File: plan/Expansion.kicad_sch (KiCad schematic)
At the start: 0 parts

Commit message: Create Expansion schematic
Expansion for GPIOs on
- Castellated Pads
- Solder Pins
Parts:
- added J2: EFR32MG24_Core_Expansion_2x6, Smarthome:Module_EFR32MG24_Core_Castellated_2x6_PTH_P2.54mm, symbol Smarthome:EFR32MG24_Core_Expansion_2x6
- added TP1, TP10, TP11, TP12, TP13, TP14, TP15, TP16, TP17, TP18, TP19, TP2, TP20, TP21, TP22, TP3, TP4, TP5, TP6, TP7, TP8, TP9: GPIO_SolderPad, Smarthome:GPIO_SolderPad_D1.0mm_Bottom, symbol Smarthome:GPIO_SolderPad
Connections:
- new net GND: J2.1 (GND)
- new net PA00: TP1.1
- new net PA01: TP2.1
- new net PA02: TP3.1
- new net PA03: TP4.1
- new net PA04: TP5.1
- new net PA05: J2.10 (PA05)
- new net PA06: TP6.1
- new net PA07: TP7.1
- new net PA08: TP8.1
- new net PA09: TP9.1
- new net PB00: TP10.1
- new net PB01: J2.5 (PB01)
- new net PB02: TP11.1
- new net PB03: J2.11 (PB03)
- new net PB04: TP12.1
- new net PB05: TP13.1
- new net PC00: J2.2 (PC00)
- new net PC01: J2.6 (PC01)
- new net PC02: J2.12 (PC02)
- new net PC03: TP14.1
- new net PC04: TP15.1
- new net PC05: J2.8 (PC05)
- new net PC06: TP16.1
- new net PC07: J2.3 (PC07)
- new net PC08: TP17.1
- new net PC09: TP18.1
- new net PD00: TP19.1
- new net PD01: TP20.1
- new net PD02: J2.9 (PD02)
- new net PD03: TP21.1
- new net PD04: TP22.1
- new net PD05: J2.4 (PD05)
- new net VBAT: J2.7 (VBAT)
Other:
- note added: "Castellated Pads + PTH GND, VBATT, GPIOs (8x EM4-Wakeup, 2x normal)"
- note added: "PAIR BUTTON"
- note added: "PORT A"
- note added: "PORT B"
- note added: "PORT C"
- note added: "PORT D"
- note added: "STATUS LED"
- note added: "SWCLK"
- note added: "SWDIO"
- note added: "SWO"
- note added: "Solder Pads"

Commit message: Added information about shared GPIOs
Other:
- note added: "PA01 - SWCLK (shared) PA02 - SWDIO (shared) PA03 - SWO (shared) PC08 - Status LED (shared) PC09 - Pair Button (shared)"
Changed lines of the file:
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@@
 	(generator_version "10.0")
 	(paper "A4")
+	(text "PA01 - SWCLK (shared)\nPA02 - SWDIO (shared)\nPA03 - SWO (shared)\nPC08 - Status LED (shared)\nPC09 - Pair Button (shared)"
+		(exclude_from_sim no)
+		(at 72.39 134.62 0)
+		(effects
+			(font
+				(size 1.27 1.27)
+			)
+			(justify left)
+		)
+	)
 	(text "PORT C"
 		(exclude_from_sim no)

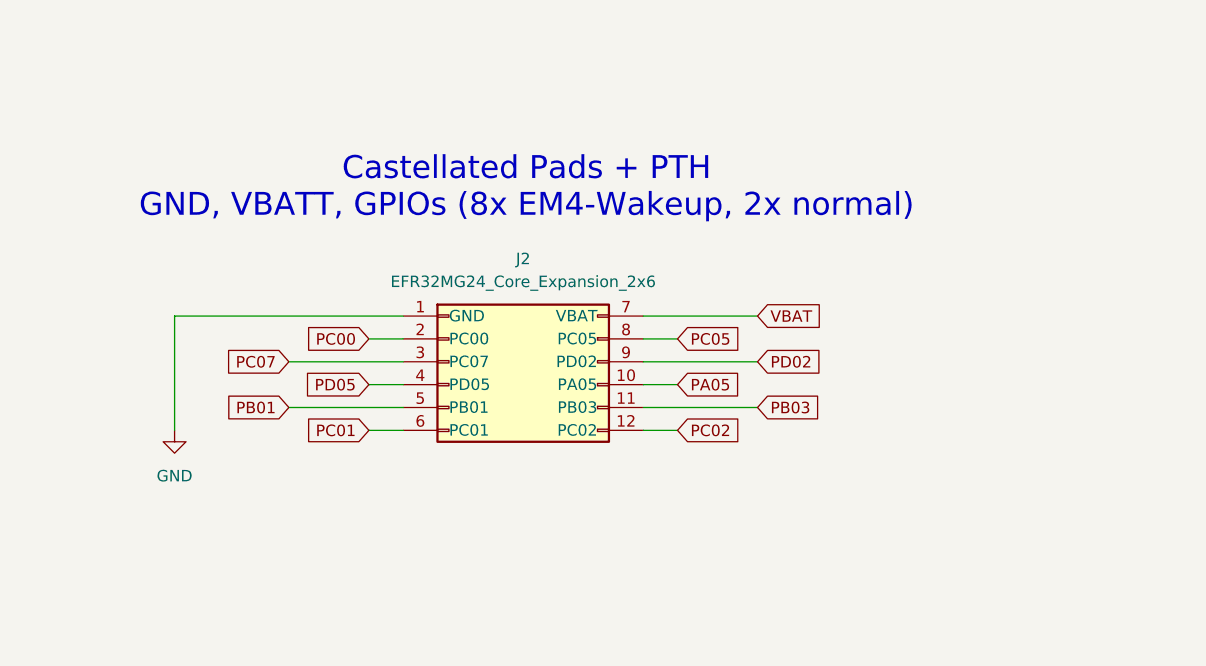
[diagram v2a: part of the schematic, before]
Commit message: Adjust and place Castellated Pads and THT connection
This implicitly defines the edge cuts of the board
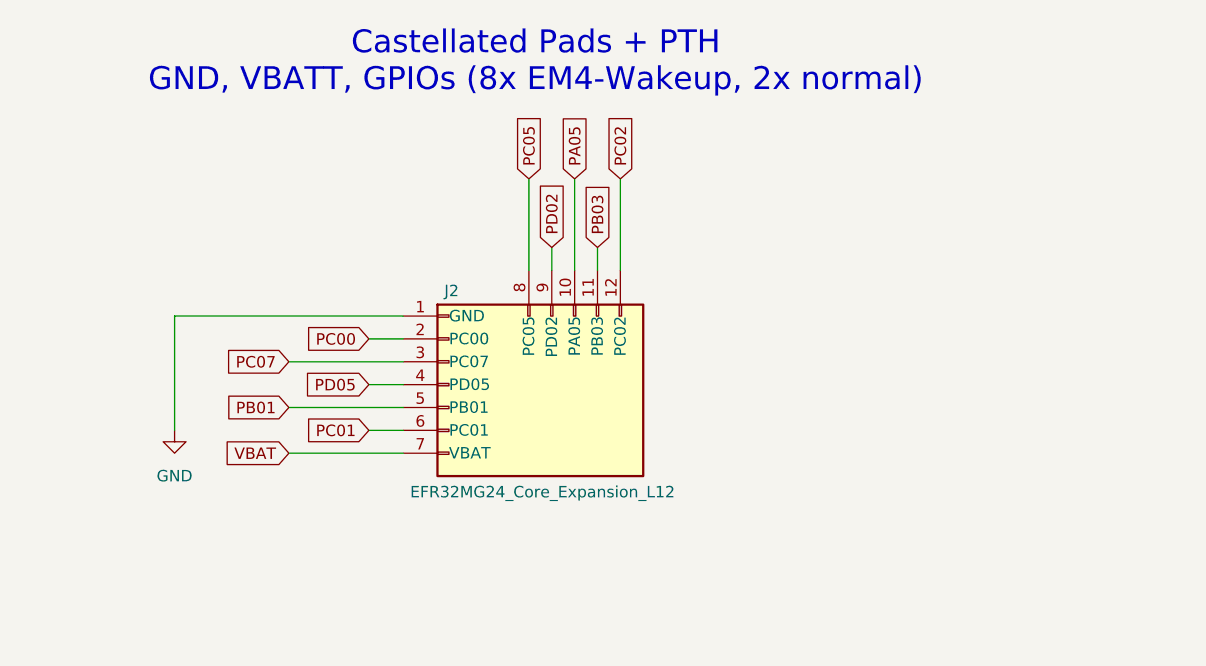
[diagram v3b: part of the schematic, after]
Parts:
- J2: value EFR32MG24_Core_Expansion_2x6 -> EFR32MG24_Core_Expansion_L12; footprint Smarthome:Module_EFR32MG24_Core_Castellated_2x6_PTH_P2.54mm -> Smarthome:Module_EFR32MG24_Core_Castellated_L_12Pin_P2.54mm; symbol Smarthome:EFR32MG24_Core_Expansion_2x6 -> Smarthome:EFR32MG24_Core_Expansion_L12
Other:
- moved on the sheet: J2
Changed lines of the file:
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@@
 	(text "Castellated Pads + PTH\nGND, VBATT, GPIOs (8x EM4-Wakeup, 2x normal)"
 		(exclude_from_sim no)
-		(at 82.296 63.246 0)
+		(at 83.312 49.276 0)
 		(effects
 			(font
@@
 	(wire
 		(pts
+			(xy 90.17 69.85) (xy 90.17 72.39)
+		)
+		(stroke
+			(width 0)
+			(type default)
+		)
+	)
+	(wire
+		(pts
 			(xy 64.77 80.01) (xy 68.58 80.01)
 		)
@@
 	(wire
 		(pts
+			(xy 85.09 69.85) (xy 85.09 72.39)
+		)
+		(stroke
+			(width 0)
+			(type default)
+		)
+	)
+	(wire
+		(pts
 			(xy 43.18 90.17) (xy 43.18 77.47)
 		)
@@
 	(wire
 		(pts
-			(xy 95.25 82.55) (xy 107.95 82.55)
+			(xy 55.88 92.71) (xy 68.58 92.71)
 		)
 		(stroke
@@
 	(wire
 		(pts
+			(xy 87.63 62.23) (xy 87.63 72.39)
+		)
+		(stroke
+			(width 0)
+			(type default)
+		)
+	)
+	(wire
+		(pts
 			(xy 181.61 88.9) (xy 185.42 88.9)
 		)
@@
 	(wire
 		(pts
-			(xy 95.25 90.17) (xy 99.06 90.17)
-		)
-		(stroke
-			(width 0)
-			(type default)
-		)
-	)
-	(wire
-		(pts
 			(xy 232.41 119.38) (xy 236.22 119.38)
 		)
@@
 	(wire
 		(pts
+			(xy 82.55 62.23) (xy 82.55 72.39)
+		)
+		(stroke
+			(width 0)
+			(type default)
+		)
+	)
+	(wire
+		(pts
 			(xy 43.18 77.47) (xy 68.58 77.47)
 		)
@@
 	(wire
 		(pts
-			(xy 95.25 80.01) (xy 99.06 80.01)
-		)
-		(stroke
-			(width 0)
-			(type default)
-		)
-	)
-	(wire
-		(pts
-			(xy 95.25 87.63) (xy 107.95 87.63)
-		)
-		(stroke
-			(width 0)
-			(type default)
-		)
-	)
-	(wire
-		(pts
 			(xy 181.61 78.74) (xy 185.42 78.74)
 		)
@@
 	(wire
 		(pts
-			(xy 95.25 85.09) (xy 99.06 85.09)
-		)
-		(stroke
-			(width 0)
-			(type default)
-		)
-	)
-	(wire
-		(pts
-			(xy 95.25 77.47) (xy 107.95 77.47)
+			(xy 92.71 62.23) (xy 92.71 72.39)
 		)
 		(stroke
@@
 	(global_label "PC02"
 		(shape input)
-		(at 99.06 90.17 0)
+		(at 92.71 62.23 90)
 		(fields_autoplaced yes)
 		(effects
@@
 		)
 		(property "Intersheetrefs" "${INTERSHEET_REFS}"
-			(at 107.0042 90.17 0)
+			(at 92.71 54.2858 90)
 			(hide yes)
 			(show_name no)
@@
 	(global_label "PD02"
 		(shape input)
-		(at 107.95 82.55 0)
+		(at 85.09 69.85 90)
 		(fields_autoplaced yes)
 		(effects
@@
 		)
 		(property "Intersheetrefs" "${INTERSHEET_REFS}"
-			(at 115.8942 82.55 0)
+			(at 85.09 61.9058 90)
 			(hide yes)
 			(show_name no)
@@
 	(global_label "PC05"
 		(shape input)
-		(at 99.06 80.01 0)
+		(at 82.55 62.23 90)
 		(fields_autoplaced yes)
 		(effects
@@
 		)
 		(property "Intersheetrefs" "${INTERSHEET_REFS}"
-			(at 107.0042 80.01 0)
+			(at 82.55 54.2858 90)
 			(hide yes)
 			(show_name no)
@@
 	(global_label "PA05"
 		(shape input)
-		(at 99.06 85.09 0)
+		(at 87.63 62.23 90)
 		(fields_autoplaced yes)
 		(effects
@@
 		)
 		(property "Intersheetrefs" "${INTERSHEET_REFS}"
-			(at 106.8228 85.09 0)
+			(at 87.63 54.4672 90)
 			(hide yes)
 			(show_name no)
@@
 	(global_label "VBAT"
 		(shape input)
-		(at 107.95 77.47 0)
+		(at 55.88 92.71 180)
+		(fields_autoplaced yes)
+		(effects
+			(font
+				(size 1.27 1.27)
+			)
+			(justify right)
+		)
+		(property "Intersheetrefs" "${INTERSHEET_REFS}"
+			(at 48.48 92.71 0)
+			(hide yes)
+			(show_name no)
+			(do_not_autoplace no)
+			(effects
+				(font
+					(size 1.27 1.27)
+				)
+				(justify right)
+			)
+		)
+	)
+	(global_label "PC06"
+		(shape input)
+		(at 181.61 129.54 180)
+		(fields_autoplaced yes)
+		(effects
+			(font
+				(size 1.27 1.27)
+			)
+			(justify right)
+		)
+		(property "Intersheetrefs" "${INTERSHEET_REFS}"
+			(at 173.6658 129.54 0)
+			(hide yes)
+			(show_name no)
+			(do_not_autoplace no)
+			(effects
+				(font
+					(size 1.27 1.27)
+				)
+				(justify right)
+			)
+		)
+	)
+	(global_label "PB03"
+		(shape input)
+		(at 90.17 69.85 90)
 		(fields_autoplaced yes)
 		(effects
@@
 		)
 		(property "Intersheetrefs" "${INTERSHEET_REFS}"
-			(at 115.35 77.47 0)
-			(hide yes)
-			(show_name no)
-			(do_not_autoplace no)
-			(effects
-				(font
-					(size 1.27 1.27)
-				)
-				(justify left)
-			)
-		)
-	)
-	(global_label "PC06"
-		(shape input)
-		(at 181.61 129.54 180)
-		(fields_autoplaced yes)
-		(effects
-			(font
-				(size 1.27 1.27)
-			)
-			(justify right)
-		)
-		(property "Intersheetrefs" "${INTERSHEET_REFS}"
-			(at 173.6658 129.54 0)
-			(hide yes)
-			(show_name no)
-			(do_not_autoplace no)
-			(effects
-				(font
-					(size 1.27 1.27)
-				)
-				(justify right)
-			)
-		)
-	)
-	(global_label "PB03"
-		(shape input)
-		(at 107.95 87.63 0)
-		(fields_autoplaced yes)
-		(effects
-			(font
-				(size 1.27 1.27)
-			)
-			(justify left)
-		)
-		(property "Intersheetrefs" "${INTERSHEET_REFS}"
-			(at 115.8942 87.63 0)
+			(at 90.17 61.9058 90)
 			(hide yes)
 			(show_name no)
@@
 	)
 	(symbol
-		(lib_id "Smarthome:EFR32MG24_Core_Expansion_2x6")
+		(lib_id "Smarthome:EFR32MG24_Core_Expansion_L12")
 		(at 73.66 82.55 0)
 		(unit 1)
@@
 		(in_pos_files yes)
 		(dnp no)
-		(fields_autoplaced yes)
 		(property "Reference" "J2"
-			(at 81.915 71.12 0)
-			(show_name no)
-			(do_not_autoplace no)
-			(effects
-				(font
-					(size 1.27 1.27)
-				)
-			)
-		)
-		(property "Value" "EFR32MG24_Core_Expansion_2x6"
-			(at 81.915 73.66 0)
-			(show_name no)
-			(do_not_autoplace no)
-			(effects
-				(font
-					(size 1.27 1.27)
-				)
-			)
-		)
-		(property "Footprint" "Smarthome:Module_EFR32MG24_Core_Castellated_2x6_PTH_P2.54mm"
+			(at 73.152 74.676 0)
+			(show_name no)
+			(do_not_autoplace no)
+			(effects
+				(font
+					(size 1.27 1.27)
+				)
+				(justify left)
+			)
+		)
+		(property "Value" "EFR32MG24_Core_Expansion_L12"
+			(at 69.342 97.028 0)
+			(show_name no)
+			(do_not_autoplace no)
+			(effects
+				(font
+					(size 1.27 1.27)
+				)
+				(justify left)
+			)
+		)
+		(property "Footprint" "Smarthome:Module_EFR32MG24_Core_Castellated_L_12Pin_P2.54mm"
 			(at 73.66 82.55 0)
 			(hide yes)
@@
 			)
 		)
-		(property "Description" "EFR32MG24 core board expansion interface, 2x6 castellated pads with optional PTH headers"
+		(property "Description" "EFR32MG24 core board expansion interface, L-shaped 12-pin castellated pads with optional PTH headers"
 			(at 87.63 82.55 0)
 			(hide yes)
